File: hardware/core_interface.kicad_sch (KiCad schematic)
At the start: 2 parts, among them J90 Core_LGA, J91 Core_LGA

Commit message: Power: +10V buck always on with battery, 10V_ENABLE removed
CIRCUIT_REVIEW B1: the LMR51430 +10V buck U3 (NSG2065Q gate drive and VTX power) was enabled by RP2354A GPIO27 over LGA pad 1 with no pull, so firmware or a Betaflight PINIO could cut ESC gate drive, and on USB-only power a high GPIO27 drove EN with VIN = 0, which the LMR51430 datasheet forbids. U3 EN is now tied to +BATT exactly like U4 (datasheet: EN may be tied to VIN; no parts added). Base: U3.5 keeps its B.Cu stub and through via, re-netted to +BATT so the via lands in the +BATT planes; the In2 run, the via and the F.Cu stub to J90 pad 1 are removed. Core: the GPIO27 route to J91 pad 1 is removed. LGA pad 1 and GPIO27 are free (no-connect); the root marker TP14 of the old net is dropped. Boards saved by pcbnew 10.0.6 without zone refill; the "Tokyo" silkscreen render caches were re-rendered with a substitute font (Tokyo not installed here).

Co-Authored-By: Claude Opus 5.5 <noreply@anthropic.com>
Claude-Session: https://claude.ai/code/session_01KTp3FLjVXfXdWrkmr6af7d
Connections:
- net 10V_ENABLE: no longer names the net of J90.1 (10V_ENABLE)
- net 10V_ENABLE: no longer J91.1 (10V_ENABLE)
- no-connect marks 0 -> 2
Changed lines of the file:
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@@
 		)
+	)
+	(no_connect
+		(at 173.99 63.5)
+	)
+	(no_connect
+		(at 72.39 63.5)
 	)
 	(bus_entry
@@
 	(wire
 		(pts
-			(xy 173.99 63.5) (xy 166.37 63.5)
-		)
-		(stroke
-			(width 0)
-			(type default)
-		)
-	)
-	(wire
-		(pts
 			(xy 173.99 83.82) (xy 166.37 83.82)
 		)
@@
 		(pts
 			(xy 173.99 119.38) (xy 166.37 119.38)
-		)
-		(stroke
-			(width 0)
-			(type default)
-		)
-	)
-	(wire
-		(pts
-			(xy 72.39 63.5) (xy 64.77 63.5)
 		)
 		(stroke
@@
 		(property "Intersheetrefs" "${INTERSHEET_REFS}"
 			(at 64.77 139.7 0)
-			(hide yes)
-			(show_name no)
-			(do_not_autoplace no)
-			(effects
-				(font
-					(size 1.27 1.27)
-				)
-			)
-		)
-	)
-	(global_label "10V_ENABLE"
-		(shape bidirectional)
-		(at 166.37 63.5 180)
-		(effects
-			(font
-				(size 1.27 1.27)
-			)
-			(justify right)
-		)
-		(property "Intersheetrefs" "${INTERSHEET_REFS}"
-			(at 166.37 63.5 0)
 			(hide yes)
 			(show_name no)
@@
 		(property "Intersheetrefs" "${INTERSHEET_REFS}"
 			(at 166.37 76.2 0)
-			(hide yes)
-			(show_name no)
-			(do_not_autoplace no)
-			(effects
-				(font
-					(size 1.27 1.27)
-				)
-			)
-		)
-	)
-	(global_label "10V_ENABLE"
-		(shape bidirectional)
-		(at 64.77 63.5 180)
-		(effects
-			(font
-				(size 1.27 1.27)
-			)
-			(justify right)
-		)
-		(property "Intersheetrefs" "${INTERSHEET_REFS}"
-			(at 64.77 63.5 0)
 			(hide yes)
 			(show_name no)
@@
 		)
 	)
-	(embedded_fonts no)
 )

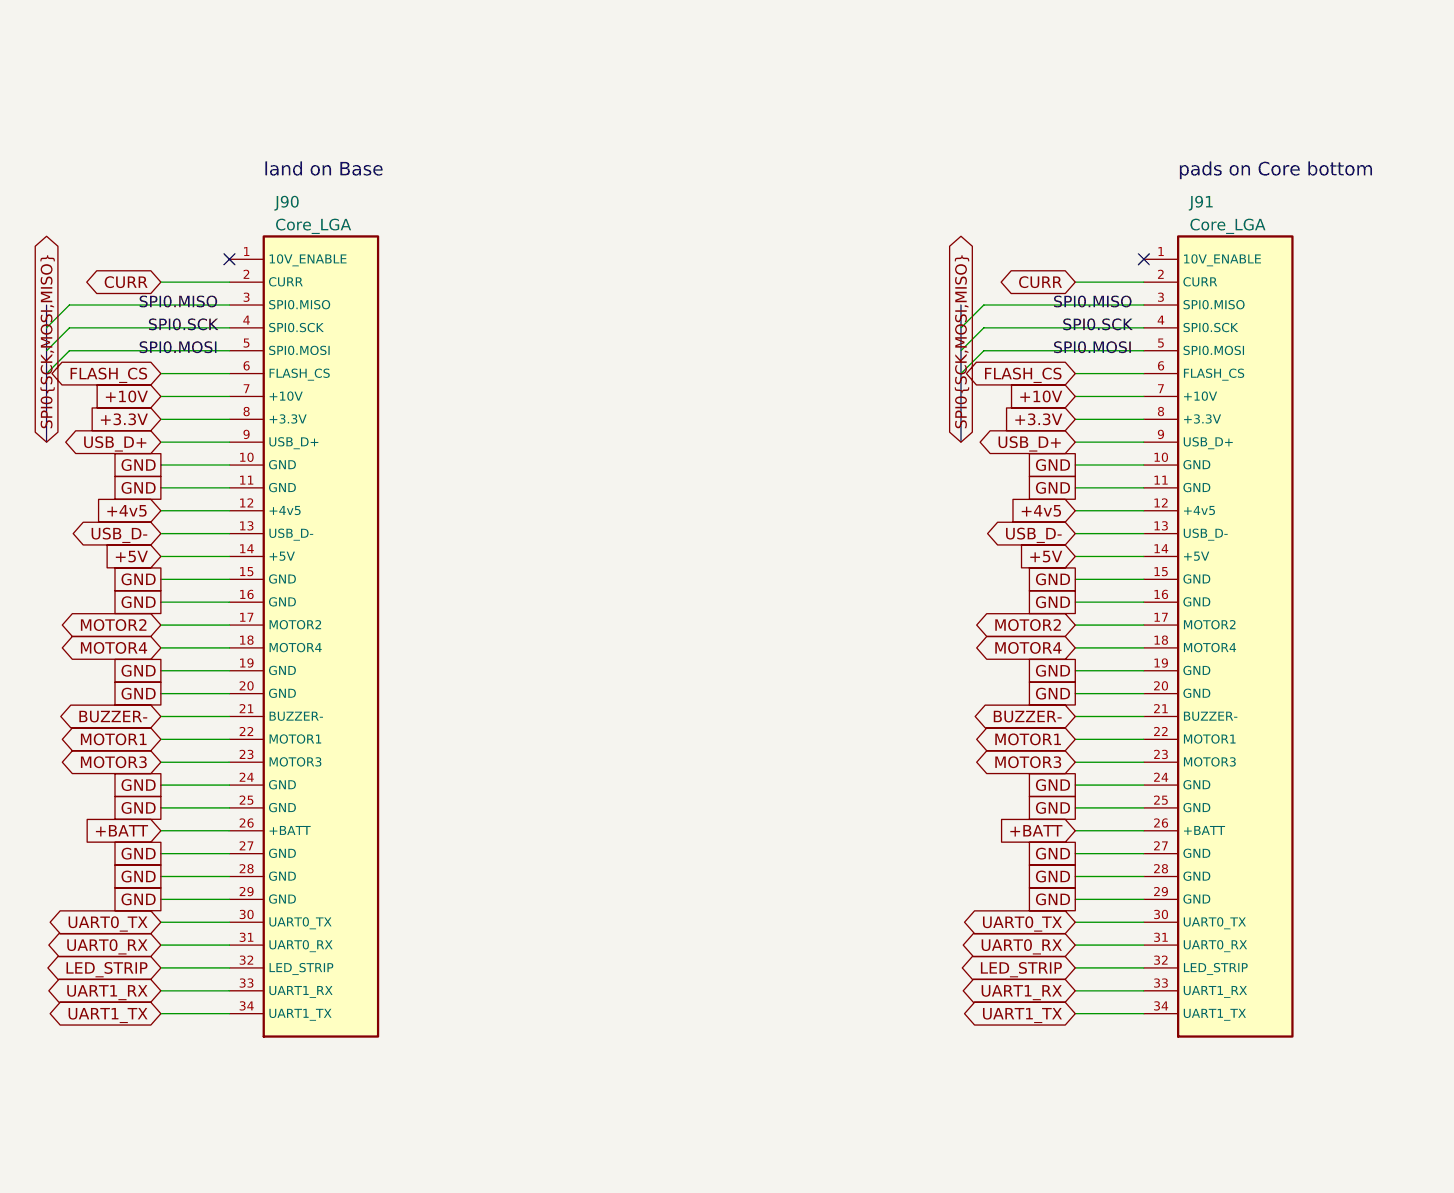
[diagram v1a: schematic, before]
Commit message: Schematic: LGA nets per the R2a spec, S1/S2/B2/D7
- LGA (core_interface, generated by tools/lga_gen.py --sheet and re-saved by
  kicad-cli): J90/J91 get the 46 pins and nets of LGA_SPEC.md. 10V_ENABLE
  (B1), +3.3V (S1) and +10V (S2) no longer cross; PU0RX, SWDIO, SWCLK do.
- B2: SH-6 U12 pin 6 (DJI SBUS) leaves UART1_RX (ESP32-C3 TX) and joins
  PU0RX (RP2354A GPIO3, PIO UART0 RX); PU0RX becomes a global net so it
  crosses the LGA.
- D7: RP2354A SWCLK/SWDIO (U2.24/.25, no-connect before) go to the LGA and
  to TP32 SWCLK / TP31 SWDIO, 0.8 mm test pads on the Base (not in the BOM).
- S2: VTX pads move to the Base next to the SH-6: J41 +10V and J51 (was a
  second +10V pad on the Core) GND, on lib:SolderPad_1.2x1.2mm.
- S1: U7 LP5912-3.3 and its caps move to the Core (board assignment is by
  footprint, see the board commit). CIN C26 becomes the 0402 1 uF 25 V
  CL05A105KA5NQNC (C52923) the spec places; the 0201 was the R1 stop-gap.
- D6/R24, the green power LED, was on +3.3V on the Base, which no longer
  exists there. Instead of moving it to the Core or deleting it (spec
  section 2), R24 now takes +3V3 (TLV75533 U23, fed from the same +4v5):
  same LED, same parts, no Core space used.

ERC: 31 errors before and after, same types (bus_to_net_conflict 3,
hier_label_mismatch 1, pin_not_connected 1, pin_not_driven 16, pin_to_pin 1,
power_pin_not_driven 9). Netlist J90/J91 checked pad by pad against
lga_spec.json: 0 mismatches.

Co-Authored-By: Claude Opus 5.5 <noreply@anthropic.com>
Claude-Session: https://claude.ai/code/session_01KTp3FLjVXfXdWrkmr6af7d
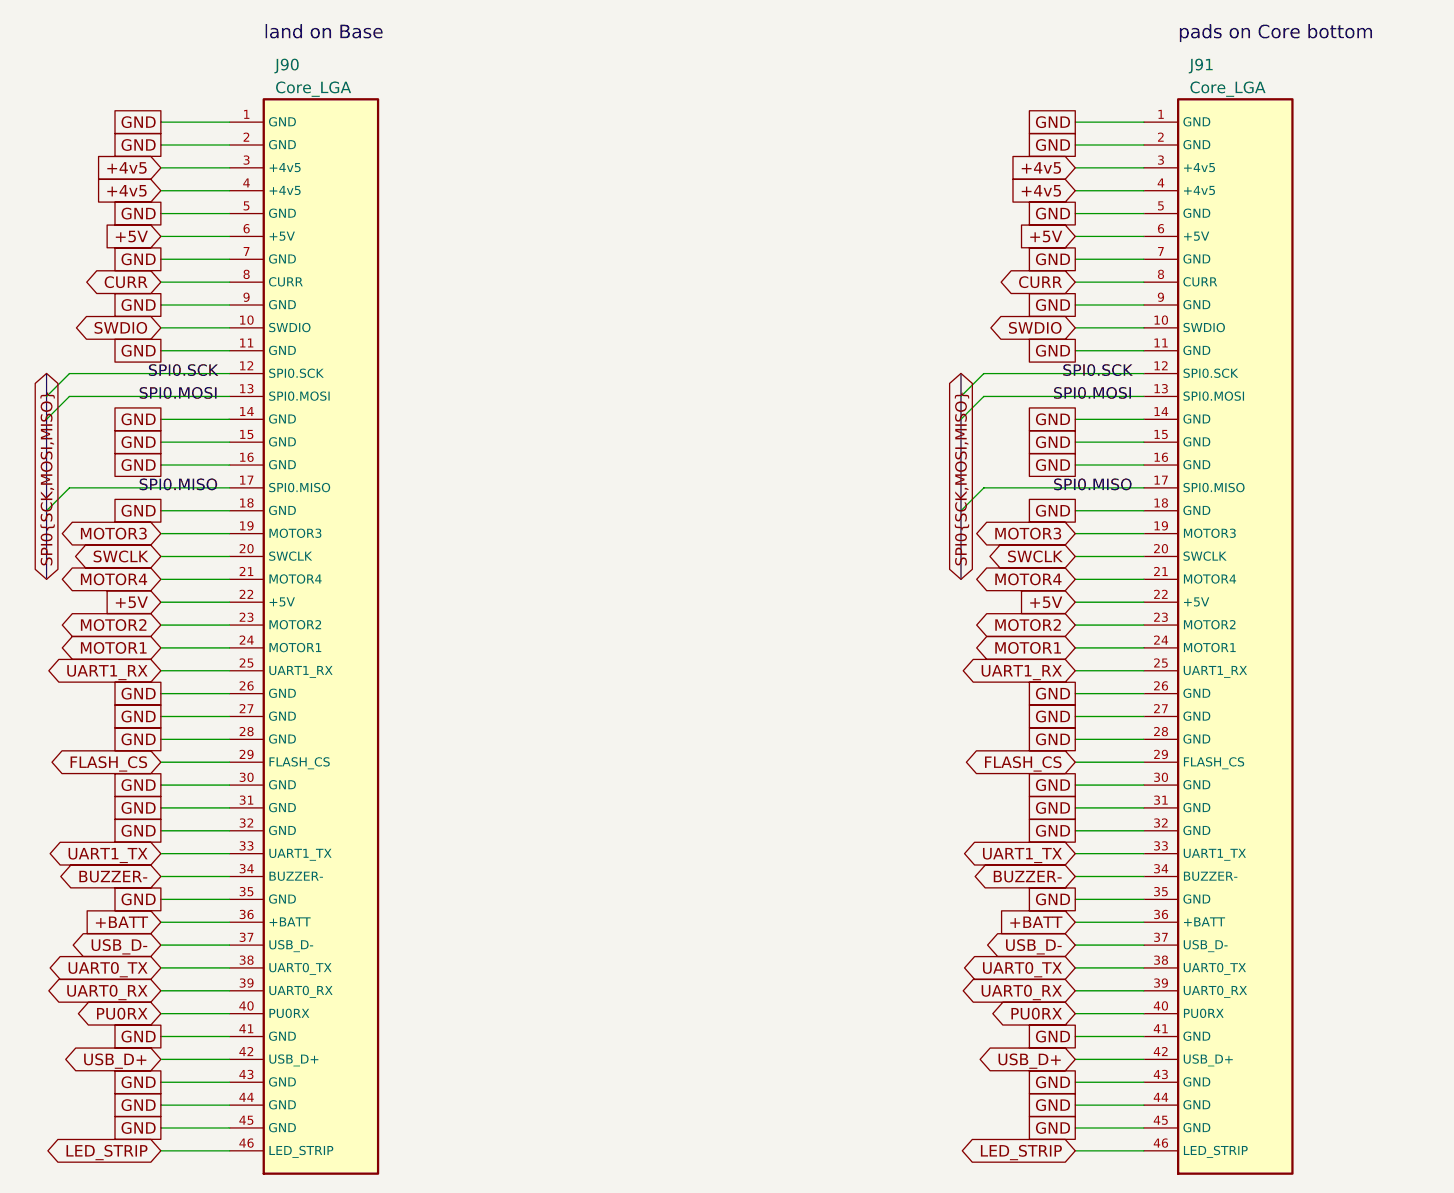
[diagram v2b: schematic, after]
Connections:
- net +10V is gone; now on net GND: J90.7 (GND), J91.7 (GND)
- net +3.3V is gone; now on net CURR: J90.8 (CURR), J91.8 (CURR)
- net +4v5: now also J90.3 (+4v5), J90.4 (+4v5), J91.3 (+4v5), J91.4 (+4v5); no longer J90.12 (+4v5), J91.12 (+4v5)
- net +5V: now also J90.22 (+5V), J90.6 (+5V), J91.22 (+5V), J91.6 (+5V); no longer J90.14 (+5V), J91.14 (+5V)
- net +BATT: now also J90.36 (+BATT), J91.36 (+BATT); no longer J90.26 (+BATT), J91.26 (+BATT)
- net BUZZER-: now also J90.34 (BUZZER-), J91.34 (BUZZER-); no longer J90.21 (BUZZER-), J91.21 (BUZZER-)
- net CURR: no longer J90.2 (CURR), J91.2 (CURR)
- net FLASH_CS: now also J90.29 (FLASH_CS), J91.29 (FLASH_CS); no longer J90.6 (FLASH_CS), J91.6 (FLASH_CS)
- net GND: now also J90.1 (GND), J90.14 (GND), J90.18 (GND), J90.2 (GND), J90.26 (GND), J90.30 (GND), J90.31 (GND), J90.32 (GND), J90.35 (GND), J90.41 (GND), J90.43 (GND), J90.44 (GND), J90.45 (GND), J90.5 (GND), J90.9 (GND), J91.1 (GND), J91.14 (GND), J91.18 (GND), J91.2 (GND), J91.26 (GND), J91.30 (GND), J91.31 (GND), J91.32 (GND), J91.35 (GND), J91.41 (GND), J91.43 (GND), J91.44 (GND), J91.45 (GND), J91.5 (GND), J91.9 (GND); no longer J90.10 (GND), J90.19 (GND), J90.20 (GND), J90.24 (GND), J90.25 (GND), J90.29 (GND), J91.10 (GND), J91.19 (GND), J91.20 (GND), J91.24 (GND), J91.25 (GND), J91.29 (GND)
- net LED_STRIP: now also J90.46 (LED_STRIP), J91.46 (LED_STRIP); no longer J90.32 (LED_STRIP), J91.32 (LED_STRIP)
- net MOTOR1: now also J90.24 (MOTOR1), J91.24 (MOTOR1); no longer J90.22 (MOTOR1), J91.22 (MOTOR1)
- net MOTOR2: now also J90.23 (MOTOR2), J91.23 (MOTOR2); no longer J90.17 (MOTOR2), J91.17 (MOTOR2)
- net MOTOR3: now also J90.19 (MOTOR3), J91.19 (MOTOR3); no longer J90.23 (MOTOR3), J91.23 (MOTOR3)
- net MOTOR4: now also J90.21 (MOTOR4), J91.21 (MOTOR4); no longer J90.18 (MOTOR4), J91.18 (MOTOR4)
- net SPI0.MISO: now also J90.17 (SPI0.MISO), J91.17 (SPI0.MISO); no longer J90.3 (SPI0.MISO), J91.3 (SPI0.MISO)
- net SPI0.MOSI: now also J90.13 (SPI0.MOSI), J91.13 (SPI0.MOSI); no longer J90.5 (SPI0.MOSI), J91.5 (SPI0.MOSI)
- net SPI0.SCK: now also J90.12 (SPI0.SCK), J91.12 (SPI0.SCK); no longer J90.4 (SPI0.SCK), J91.4 (SPI0.SCK)
- net UART0_RX: now also J90.39 (UART0_RX), J91.39 (UART0_RX); no longer J90.31 (UART0_RX), J91.31 (UART0_RX)
- net UART0_TX: now also J90.38 (UART0_TX), J91.38 (UART0_TX); no longer J90.30 (UART0_TX), J91.30 (UART0_TX)
- net UART1_RX: now also J90.25 (UART1_RX), J91.25 (UART1_RX); no longer J90.33 (UART1_RX), J91.33 (UART1_RX)
- net UART1_TX: now also J90.33 (UART1_TX), J91.33 (UART1_TX); no longer J90.34 (UART1_TX), J91.34 (UART1_TX)
- net USB_D+: now also J90.42 (USB_D+), J91.42 (USB_D+); no longer J90.9 (USB_D+), J91.9 (USB_D+)
- net USB_D-: now also J90.37 (USB_D-), J91.37 (USB_D-); no longer J90.13 (USB_D-), J91.13 (USB_D-)
- new net PU0RX: J90.40 (PU0RX), J91.40 (PU0RX)
- new net SWCLK: J90.20 (SWCLK), J91.20 (SWCLK)
- new net SWDIO: J90.10 (SWDIO), J91.10 (SWDIO)
- no-connect marks 2 -> 0
